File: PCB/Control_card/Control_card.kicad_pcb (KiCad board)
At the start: 2 copper layers, 24 parts, among them IC1 TLSR8253F512ET48, J1 Conn_02x04_Counter_Clockwise

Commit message: Ajout crystal
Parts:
- added Y1: Crystal_GND24, Touch_Switch_Custom:Crystal, F.Cu at (115.7, 57.4)
- moved J1 24.7 mm to (102.2, 91.6), turned to 90 degrees
- moved U1 1.64 mm to (125.3, 45.8)
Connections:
- IC1 pad 2: unconnected-(IC1-PA0-Pad2) -> In1
- IC1 pad 3: unconnected-(IC1-PA1-Pad3) -> In2
- IC1 pad 4: unconnected-(IC1-PA2-Pad4) -> In3
- IC1 pad 5: unconnected-(IC1-PA3-Pad5) -> In4
- L2 pad 1: Net-(IC1-VDCDC_SW) -> Net-(IC1-VDCDC)
- L2 pad 2: Net-(IC1-VDCDC) -> Net-(IC1-VDCDC_SW)
- U1 pad 10: Relay3 -> CT3
- U1 pad 11: Relay4 -> CT4
- U1 pad 8: Relay1 -> CT1
- U1 pad 9: Relay2 -> CT2
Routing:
- net (no net): track 0.00 -> 3.08 mm

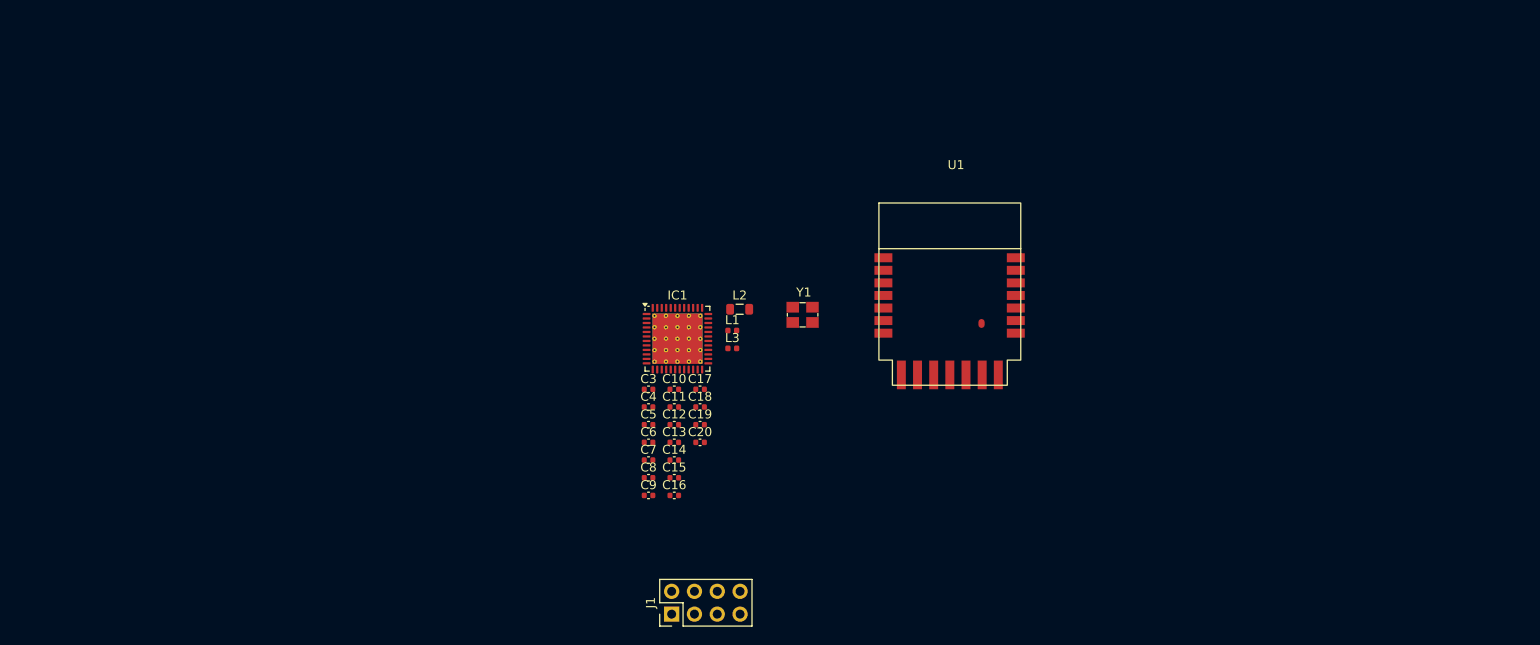
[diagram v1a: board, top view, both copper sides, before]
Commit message: Continuation routage & ajout antenne
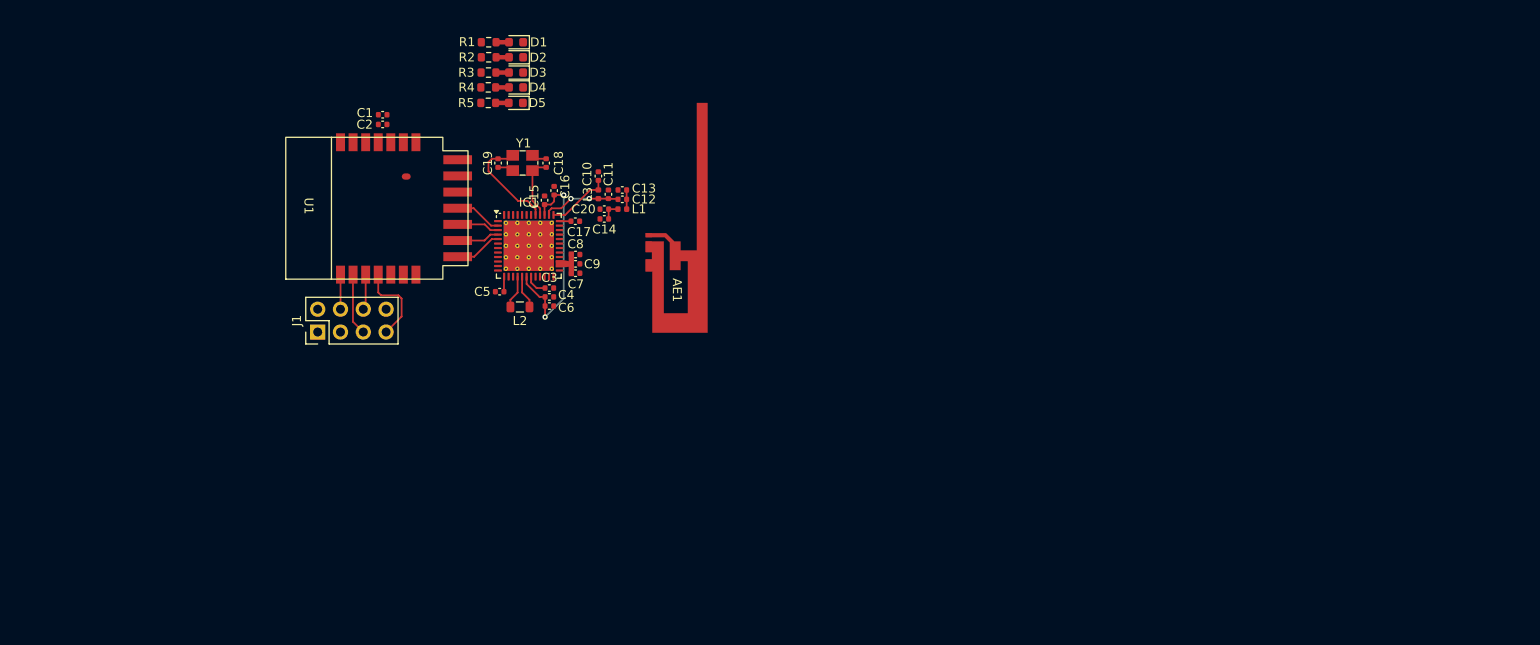
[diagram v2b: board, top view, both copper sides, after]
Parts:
- added AE1: Antenna, Touch_Switch_Custom:Antenna, F.Cu at (110.3, 49.2)
- added C1: 10u, Capacitor_SMD:C_0402_1005Metric, F.Cu at (70.1, 36.0)
- added C2: 0,1u, Capacitor_SMD:C_0402_1005Metric, F.Cu at (70.1, 37.1)
- added D1: LED, LED_SMD:LED_0603_1608Metric, F.Cu at (84.9, 27.9)
- added D2: LED, LED_SMD:LED_0603_1608Metric, F.Cu at (84.9, 29.6)
- added D3: LED, LED_SMD:LED_0603_1608Metric, F.Cu at (84.9, 31.3)
- added D4: LED, LED_SMD:LED_0603_1608Metric, F.Cu at (84.9, 32.9)
- added D5: LED, LED_SMD:LED_0603_1608Metric, F.Cu at (84.9, 34.7)
- added R1: R, Resistor_SMD:R_0603_1608Metric, F.Cu at (81.9, 27.9)
- added R2: R, Resistor_SMD:R_0603_1608Metric, F.Cu at (81.9, 29.6)
- added R3: R, Resistor_SMD:R_0603_1608Metric, F.Cu at (81.8, 31.3)
- added R4: R, Resistor_SMD:R_0603_1608Metric, F.Cu at (81.8, 32.9)
- added R5: R, Resistor_SMD:R_0603_1608Metric, F.Cu at (81.8, 34.7)
- C20: value 1u -> 0,5p
- moved U1 66.6 mm to (59.3, 54.3), turned to 90 degrees
- moved J1 50.4 mm to (62.8, 60.2)
- moved C19 36.8 mm to (82.9, 41.4), turned to -90 degrees
- moved C16 36.5 mm to (89.2, 44.5), turned to 90 degrees
- moved Y1 35.5 mm to (84.5, 40.5)
- moved C15 34.1 mm to (88.1, 45.5), turned to 90 degrees
- moved C18 32.1 mm to (88.3, 41.4), turned to 90 degrees
- moved C13 28.7 mm to (96.7, 44.4), turned to 180 degrees
- moved C20 28.1 mm to (94.7, 46.5), turned to 180 degrees
- moved C14 28.0 mm to (94.7, 47.6), turned to 180 degrees
- moved C9 27.0 mm to (91.5, 52.6)
- moved C8 26.2 mm to (91.5, 51.6)
- moved C12 25.8 mm to (96.7, 45.4)
- moved C10 25.2 mm to (94.1, 42.8), turned to 90 degrees
- moved C11 24.8 mm to (95.2, 44.9), turned to 90 degrees
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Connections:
- C14 pad 1: Antenna -> Net-(AE1-A)
- C20 pad 1: Reset -> Net-(AE1-A)
- IC1 pad 2: In1 -> In4
- IC1 pad 3: In2 -> In3
- IC1 pad 4: In3 -> In2
- IC1 pad 49: (no net) -> GND
- IC1 pad 5: In4 -> In1
- J1 pad 1: unconnected-(J1-Pin_1-Pad1) -> 3.3V
- J1 pad 2: CT4 -> GND
- J1 pad 3: CT3 -> unconnected-(J1-Pin_3-Pad3)
- J1 pad 4: CT2 -> CT1
- J1 pad 5: CT1 -> CT2
- J1 pad 6: unconnected-(J1-Pin_6-Pad6) -> CT3
- J1 pad 7: GND -> CT4
- J1 pad 8: 3.3V -> unconnected-(J1-Pin_8-Pad8)
- L1 pad 2: Antenna -> Net-(AE1-A)
- U1 pad 1: In1 -> CT1
- U1 pad 10: CT3 -> In3
- U1 pad 11: CT4 -> In4
- U1 pad 2: In2 -> CT2
- U1 pad 3: In3 -> CT3
- U1 pad 4: In4 -> CT4
- U1 pad 8: CT1 -> In1
- U1 pad 9: CT2 -> In2
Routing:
- net VVD1V2: track 0.00 -> 24.3 mm, vias 0 -> 2
- net XC2: track 0.00 -> 11.7 mm
- net CT4: track 0.00 -> 9.32 mm
- net ANT: track 0.00 -> 8.74 mm, vias 0 -> 2
- net Net-(IC1-VANT): track 0.00 -> 7.22 mm
- net XC1: track 0.00 -> 6.96 mm
- net CT2: track 0.00 -> 6.87 mm
- net In1: track 0.00 -> 5.30 mm
- net In4: track 0.00 -> 5.29 mm
- net In2: track 0.00 -> 4.76 mm
- net In3: track 0.00 -> 4.75 mm
- net CT3: track 0.00 -> 3.96 mm
- net CT1: track 0.00 -> 3.85 mm
- net Net-(IC1-VDCDC): track 0.00 -> 3.72 mm
- net Net-(IC1-VDCDC_SW): track 0.00 -> 3.71 mm
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
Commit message: Routage
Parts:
- AE1: value Antenna -> Antenna_Shield
- D1, D2, D3, D4, D5: footprint LED_SMD:LED_0603_1608Metric -> LED_SMD:LED_0805_2012Metric
- J1: moved to B.Cu
- moved AE1 71.6 mm to (42.4, 71.9), turned to 180 degrees
- moved L1 51.0 mm to (47.9, 61.2)
- moved C20 50.8 mm to (45.8, 60.2)
- moved C14 50.8 mm to (45.8, 61.2)
- moved C13 50.0 mm to (49.5, 60.8), turned to 90 degrees
- moved C12 48.2 mm to (51.2, 61.2), turned to 180 degrees
- moved C11 45.3 mm to (52.8, 60.8)
- moved C8 44.1 mm to (47.7, 56.7), turned to 180 degrees
- moved L3 42.8 mm to (54.5, 61.2), turned to 180 degrees
- moved C10 41.7 mm to (56.6, 61.2), turned to 0 degrees
- moved C5 37.6 mm to (45.5, 55.2)
- moved C7 36.3 mm to (55.3, 55.0), turned to -90 degrees
- moved C9 36.3 mm to (55.3, 52.3), turned to 90 degrees
- moved C17 35.8 mm to (55.8, 49.0)
- moved C3 35.8 mm to (52.9, 56.5)
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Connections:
- U1 pad 1: CT1 -> In1
- U1 pad 10: In3 -> CT3
- U1 pad 11: In4 -> CT4
- U1 pad 2: CT2 -> In2
- U1 pad 3: CT3 -> In3
- U1 pad 4: CT4 -> In4
- U1 pad 8: In1 -> CT1
- U1 pad 9: In2 -> CT2
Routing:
- net 3.3V: track 0.00 -> 87.7 mm, vias 0 -> 6
- net GND: track 3.47 -> 68.3 mm, vias 0 -> 33
- net OutLed1: track 0.00 -> 20.5 mm
- net OutLed2: track 0.00 -> 19.8 mm
- net OutLed3: track 0.00 -> 18.6 mm, vias 0 -> 2
- net ANT: track 8.74 -> 26.8 mm
- net CT3: track 3.96 -> 21.4 mm, vias 0 -> 1
- net OutLed4: track 0.00 -> 15.8 mm, vias 0 -> 2
- net CT2: track 6.87 -> 22.0 mm, vias 0 -> 1
- net CT1: track 3.85 -> 18.8 mm, vias 0 -> 1
- net Net-(IC1-VANT): track 7.22 -> 18.6 mm
- net CT4: track 9.32 -> 20.4 mm, vias 0 -> 1
- net In1: track 5.30 -> 15.7 mm
- net In2: track 4.76 -> 14.0 mm
- net In3: track 4.75 -> 12.4 mm
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- added copper zone on B.Cu, net GND
- added copper zone on F.Cu, net GND
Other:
- board outline added: 31.1 x 44.3 mm

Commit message: Finalisation carte contrôle
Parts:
- moved C8 0.67 mm to (47.1, 56.7)
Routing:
- net OutLed2: track 19.8 -> 22.2 mm
- net Net-(IC1-VANT): track 18.6 -> 20.9 mm
- net OutLed1: track 20.5 -> 22.5 mm
- net GND: track 68.3 -> 69.4 mm
- net ANT: track 26.8 -> 26.1 mm

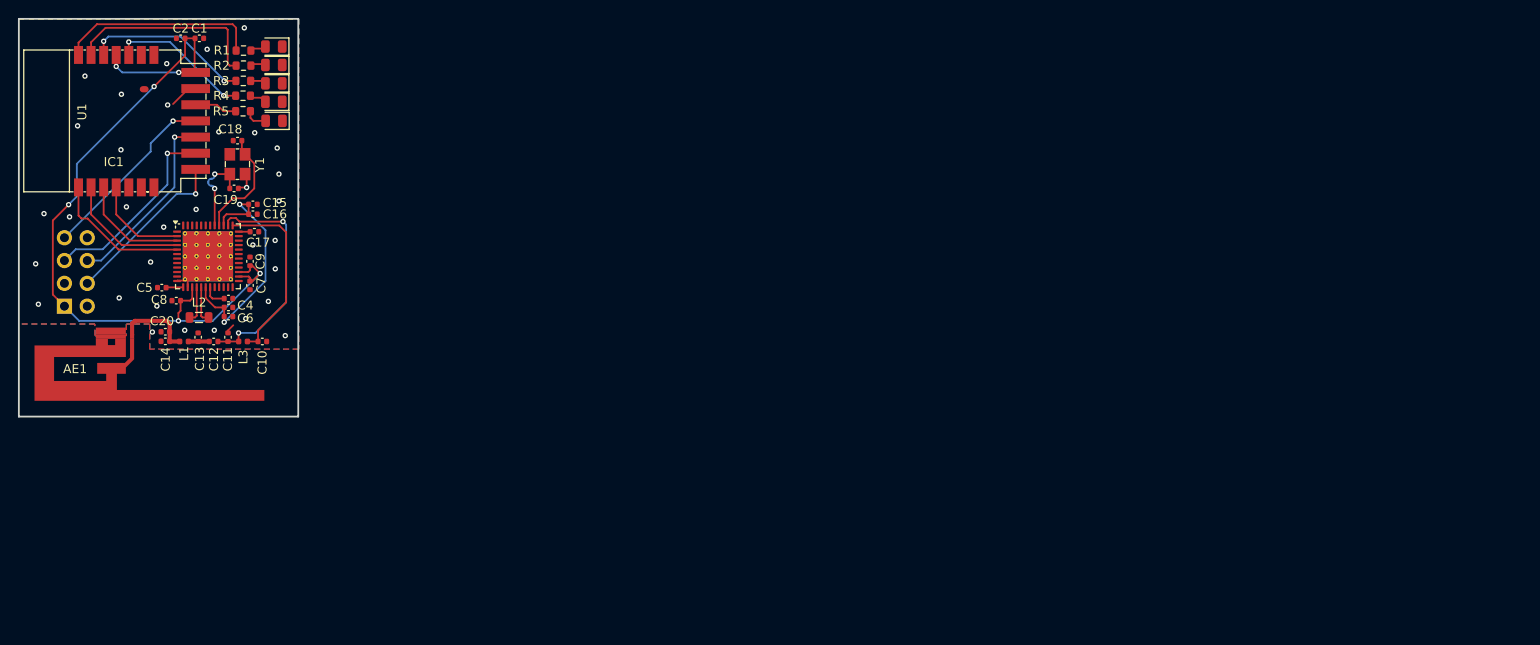
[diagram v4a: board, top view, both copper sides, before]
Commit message: Ajout des touch switch
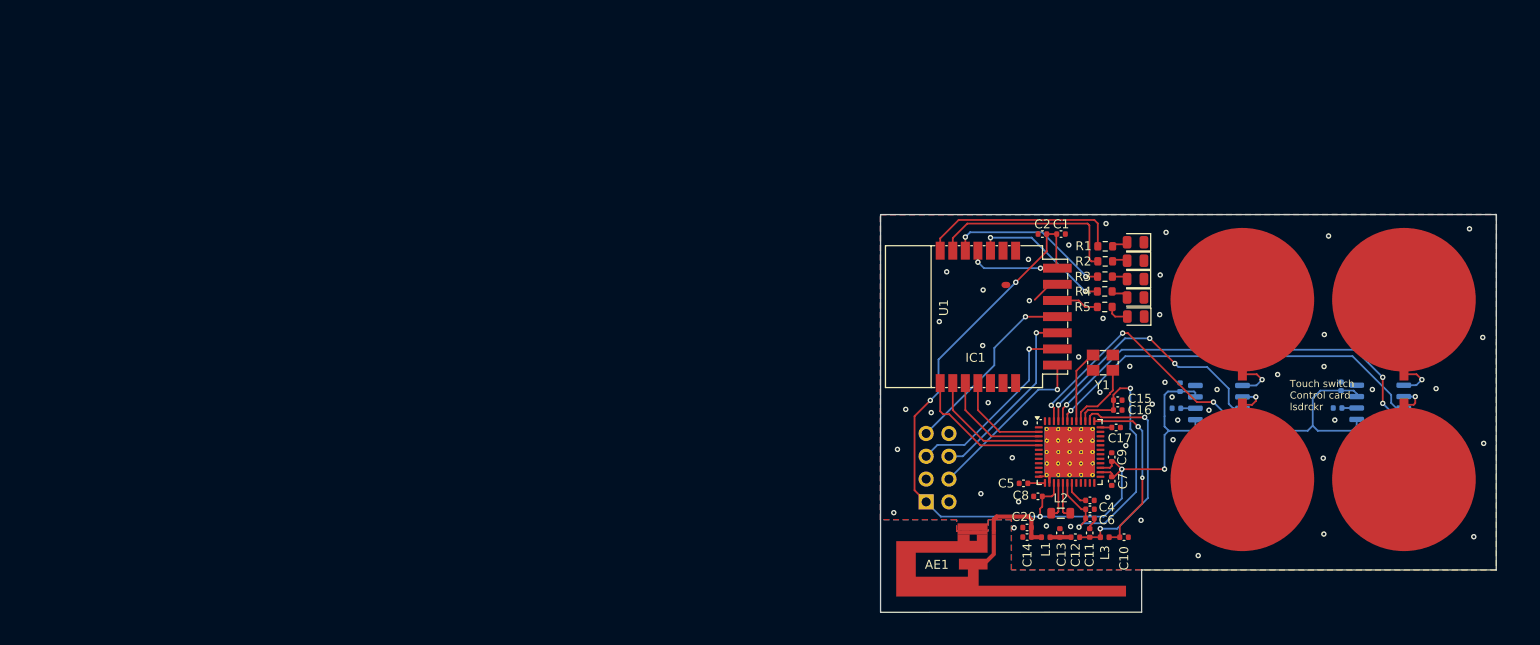
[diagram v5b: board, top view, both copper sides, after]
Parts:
- removed C18, C19: NC, Capacitor_SMD:C_0402_1005Metric
- added C21: 0,1u, Capacitor_SMD:C_0402_1005Metric, B.Cu at (176.8, 66.2)
- added C22: 0,01u, Capacitor_SMD:C_0402_1005Metric, B.Cu at (176.4, 68.7)
- added C23: 0,01u, Capacitor_SMD:C_0402_1005Metric, B.Cu at (158.5, 68.7)
- added C24: 0,1u, Capacitor_SMD:C_0402_1005Metric, B.Cu at (158.9, 66.3)
- added J2: Conn_01x01_Pin, Touch_Switch_Custom:Touch Switch, F.Cu at (183.8, 56.6)
- added J3: Conn_01x01_Pin, Touch_Switch_Custom:Touch Switch, F.Cu at (183.8, 76.6)
- added J4: Conn_01x01_Pin, Touch_Switch_Custom:Touch Switch, F.Cu at (165.8, 56.6)
- added J5: Conn_01x01_Pin, Touch_Switch_Custom:Touch Switch, F.Cu at (165.8, 76.6)
- added U2: ~, Package_SO:SOP-8_3.9x4.9mm_P1.27mm, B.Cu at (181.2, 68.0)
- added U3: ~, Package_SO:SOP-8_3.9x4.9mm_P1.27mm, B.Cu at (163.2, 68.1)
- moved C15 98.8 mm to (151.9, 67.8)
- moved C16 98.8 mm to (151.9, 68.9)
- moved C3 98.6 mm to (148.8, 79.0)
- moved C4 98.6 mm to (148.8, 79.9)
- moved C6 98.6 mm to (148.8, 81.0)
- moved AE1 98.4 mm to (138.3, 93.7)
- moved C1 98.4 mm to (145.6, 49.3)
- moved C10 98.4 mm to (152.6, 83.1)
- moved C12 98.4 mm to (147.2, 83.1)
- moved C13 98.4 mm to (145.5, 82.6)
- moved C14 98.4 mm to (141.8, 83.0)
- moved C17 98.4 mm to (151.8, 70.8)
- moved C2 98.4 mm to (143.5, 49.3)
- moved C20 98.4 mm to (141.8, 82.0)
- moved C7 98.4 mm to (151.3, 76.8)
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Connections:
- IC1 pad 43: unconnected-(IC1-PD1-Pad43) -> OutSw1
- IC1 pad 44: unconnected-(IC1-PD2-Pad44) -> OutSw2
- IC1 pad 45: unconnected-(IC1-PD3-Pad45) -> OutSw3
- IC1 pad 46: unconnected-(IC1-PD4-Pad46) -> OutSw4
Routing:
- net 3.3V: track 88.0 -> 139.8 mm, vias 6 -> 7
- net OutSw2: track 0.00 -> 47.0 mm, vias 0 -> 3
- net OutSw1: track 0.00 -> 43.9 mm, vias 0 -> 1
- net OutSw4: track 0.00 -> 30.6 mm, vias 0 -> 3
- net OutSw3: track 0.00 -> 29.6 mm, vias 0 -> 3
- net VVD1V2: track 27.5 -> 34.2 mm
- net Net-(J4-Pin_1): track 0.00 -> 4.90 mm, vias 0 -> 1
- net Net-(J2-Pin_1): track 0.00 -> 4.52 mm, vias 0 -> 1
- net XC1: track 11.9 -> 7.84 mm
- net Net-(J5-Pin_1): track 0.00 -> 3.62 mm, vias 0 -> 1
- net Net-(J3-Pin_1): track 0.00 -> 3.34 mm, vias 0 -> 1
- net Net-(U2-VC): track 0.00 -> 1.65 mm
- net Net-(U3-VC): track 0.00 -> 1.63 mm
- net XC2: track 9.82 -> 8.20 mm, vias 2 -> 0
- net Net-(IC1-VANT): track 20.9 -> 19.9 mm, vias 0 -> 2
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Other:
- board size 31.1 x 44.3 mm -> 68.6 x 44.3 mm
- board text added: "Touch switch Control card lsdrckr"

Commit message: Routage
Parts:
- J2, J3, J4, J5: footprint Touch_Switch_Custom:Touch Switch -> Touch_Switch_Custom:TouchSwitch
- moved C8 0.25 mm to (143.2, 78.3)
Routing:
- net 3.3V: track 139.8 -> 276.3 mm, vias 7 -> 9
- net OutSw3: track 29.6 -> 34.8 mm
- net OutSw1: track 43.9 -> 48.9 mm
- net OutSw4: track 30.6 -> 35.3 mm
- net OutSw2: track 47.0 -> 51.7 mm
- net VVD1V2: track 34.2 -> 34.8 mm
- net CT2: track 22.0 -> 22.5 mm
- net GND: vias 51 -> 52
